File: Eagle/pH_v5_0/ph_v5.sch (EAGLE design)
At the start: 89 parts, among them CON1 JACK_DC_BARREL, IC1 MCP1703DB, J1 RJ12RIGHTANGLE-I2C, J2 RJ12RIGHTANGLE-I2C, Q5 BSP75, Q6 BSP75, U1 HX711, X2 16MHz, X3 FH12-08S-1SH, X4 MINI-USB

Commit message: new v4.3, removed bistable control of the stepper, now on pins A0/A1/D8/D9, control sequence must be adapted in the arduino code. Started to work on the ph_V5.0 board, need to add two steppers and the analog backend circuit
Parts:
- removed 5V1: (no value), Headerlibrary:PINHD-1X1
- removed C16, C17: 100nF, rcl:C-EUC1206
- removed CU5, CU6: 10uF, rcl:C-EUC1206
- removed D3, D5: 1N581D1206, lpatiny:1N581D1206
- removed IN, OUT: (no value), jumper:JP1E
- removed LDIN, LDOUT, LDPW5: RED, adafruit:LEDCHIP-LED0805
- removed Q5, Q6: BSP75, infineon:BSP613P
- removed R13: 1k, resistor:R-EU_R0805
- removed R5, R6, R8: 1K, rcl:R-EU_R0805
- removed U$2: NCP1117LPST50T3G, lpatiny:NCP1117LPST50T3G
- removed U$6: TXB0104, lpatiny:TXB0104
- added 100K: 100k, rcl:R-EU_R0805
- added AN_OUT, LORA_RST: (no value), Headerlibrary:PINHD-1X1
- added C3, C4: 100nF, rcl:C-EUC1206
- added JP2: M02PTH, SparkFun-Connectors:M02PTH
- added LDM1, LDM2, LDM3, LDM4, RXLD, TXLD: RED, adafruit:LEDCHIP-LED0805
- added Q1, Q2, Q3, Q4: BSP75, infineon:BSP613P
- added R10: 1K, rcl:R-EU_R0805
- added RK10, RK11, RK14, RK17, RK8, RK9: 10K, rcl:R-EU_R0805
- added RK15, RK16: 10k, rcl:R-EU_R0805
- added RT2: 4.7k, resistor:R-EU_R1206
- added SJ4, SJ5, SJ6: JUMPER-PAD-2-NC_BY_TRACE, SparkFun-Passives:JUMPER-PAD-2-NC_BY_TRACE
- added STEPPER: (no value), con-lsta:FE06-1
- added U$4: DS18B20, lpatiny:DS18B20
- added U100: RN2483, Octanis1:RN2483
- RK12, RK13: value 10k -> 10K
- X2: value 16MHz -> 8MHz
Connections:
- removed net +5V: CU5.1, D3.A, U$2.OUT, U$2.TAB_OUT
- removed net +5V/1: 32U4.AVCC, 32U4.AVCC1, 32U4.UVCC, 32U4.VCC, 32U4.VCC1, 5V1.1, BJ1.E, C1.1, C12.2, C17.2, C2.1, C6.1, CU1.1, CU3.1, CU4.1, CU7.1, D2.C, D3.C, D4.C, IC1.VI, J1.5, J2.5, R13.1, R8.2, RK1.1, RK18.1, RK19.1, RK2.1, RK5.2, RK6.2, U$6.VCCB, U1.DVDD, U1.VSUP, X3-1.1, X3-2.1
- removed net FMOSI: D5.A, RK4.1, U$1.MOSI
- removed net MISO3: U$1.MISO, U$6.A3
- removed net MOSI3: D5.C, U$6.A2
- removed net N$11: Q5.G, R6.2, RK13.2
- removed net N$12: LDPW5.A, R13.2
- removed net N$13: OUT.2, Q5.D@1
- removed net N$17: IN.2, Q6.D@1
- removed net N$27: LDIN.A, RK12.1
- removed net N$28: LDOUT.A, RK13.1
- removed net N$4: R8.1, U$6.OE
- removed net N$8: Q6.G, R5.2, RK12.2
- removed net SCK3: RK3.1, U$6.A4
- removed net SC_MEM: R3.2, U$6.NC
- new net ANGND: C3.2, C4.2, SJ4.2, SJ5.2, SJ6.2, U100.P$1, U100.P$11, U100.P$20, U100.P$21, U100.P$22, U100.P$24, U100.P$26, U100.P$27, U100.P$28, U100.P$33, U100.P$41, U100.P$47, U100.P$8
- new net ANT868: AN_OUT.1, U100.P$23
- new net B+: JP2.1, U1.INB+
- new net B-: JP2.2, U1.INB-
- new net N$14: Q4.D@1, RK8.1, STEPPER.1
- new net N$15: Q2.D@1, RK9.1, STEPPER.3
- new net N$16: Q3.D@1, RK10.1, STEPPER.4
- new net N$18: RK15.2, TXLD.A
- new net N$19: Q1.D@1, RK11.1, STEPPER.6
- new net N$24: RK16.2, RXLD.A
- new net N$31: LDM4.C, RK8.2
- new net N$32: LDM3.C, RK9.2
- new net N$33: LDM2.C, RK10.2
- new net N$37: LDM1.C, RK11.2
- new net N$9: R10.2, RT2.2, U$4.DQ
- net +12V: now also C1.1, C2.1, CU3.1, CU4.1, CU7.1, D2.C, D4.C, IC1.VI, LDM1.A, LDM2.A, LDM3.A, LDM4.A, STEPPER.2, STEPPER.5, X3-1.1, X3-2.1; no longer CU6.1, IN.1, OUT.1, U$2.IN
- net 3.3V: now also 100K.1, 32U4.AVCC, 32U4.AVCC1, 32U4.UVCC, 32U4.VCC, 32U4.VCC1, BJ1.E, C12.2, C3.1, C4.1, C6.1, CU1.1, RK1.1, RK15.1, RK16.1, RK18.1, RK19.1, RK2.1, RK5.2, RK6.2, RT2.1, U$4.VDD, U1.DVDD, U1.VSUP, U100.P$12, U100.P$34; no longer C16.2, U$6.VCCA
- net A0: now also Q2.G, RK13.2
- net A1: now also Q4.G, RK17.2
- net A2: now also Q3.G, RK14.2; no longer R5.1
- net A3: now also Q1.G, RK12.2; no longer R6.1
- net D10*: now also R3.2; no longer U$6.NC2
- net D5*: now also 100K.2, LORA_RST.1, U100.P$32
- net D6*: now also R10.1
- net GND: now also Q1.S, Q2.S, Q3.S, Q4.S, RK12.1, RK13.1, RK14.1, RK17.1, SJ4.1, SJ5.1, SJ6.1, U$4.GND; no longer C16.1, C17.1, CU5.2, CU6.2, LDIN.C, LDOUT.C, LDPW5.C, Q5.S, Q6.S, U$2.ADJ, U$6.GND
- net MISO: now also U$1.MISO; no longer U$6.B3
- net MOSI: now also RK4.1, U$1.MOSI; no longer U$6.B2
- net RX: now also U100.P$6
- net RXLED: now also RXLD.C
- net SCK: now also RK3.1; no longer U$6.B4
- net TX: now also U100.P$7
- net TXLED: now also TXLD.C
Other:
- note added: "LoRa RN2483"
- note added: "One wire"
- note added: "STEPPER"
- note removed: "5V LDO"
- note removed: "FOOD"
- note removed: "LEVEL_Converters"
- note removed: "PID"
- moved on the sheet: CU9, RK12, RK13, RUSB1, RUSB2, X4G$1

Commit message: started design of the phv5.0 board, conductommetry is still missing, stepper to be rerouted to use one single port would be better !
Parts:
- removed C9: 100nF, rcl:C-EUC1206
- removed JP2: M02PTH, SparkFun-Connectors:M02PTH
- removed R10: 1K, rcl:R-EU_R0805
- removed RL1, RL2: 100, resistor:R-EU_M0805
- removed RT2: 4.7k, resistor:R-EU_R1206
- removed U$4: DS18B20, lpatiny:DS18B20
- removed WGT: (no value), SparkFun-Connectors:M05PTH
- added C14, C15: 100n, rcl:C-EUC1206
- added C16: 22uF, rcl:C-EUC1206
- added IC2: TL084D, linear:TL084D
- added LDM5, LDM6, LDM7, LDM8: RED, adafruit:LEDCHIP-LED0805
- added Q5, Q6, Q7, Q8: BSP75, infineon:BSP613P
- added R4, R5, R9: 2.2k, resistor:R-EU_R0805
- added R6, R8: 100k, resistor:R-EU_R0805
- added STEPPER1: (no value), con-lsta:FE06-1
- added U$2: BNC-VERTICAL, phMeter:BNC-VERTICAL
- added U$3: VERTICAL-JACK, phMeter:VERTICAL-JACK
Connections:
- removed net N$20: C9.2, RL1.1, U1.INA-
- removed net N$43: C9.1, RL2.1, U1.INA+
- new net N$11: LDM6.C, RK13.2
- new net N$12: LDM7.C, RK14.2
- new net N$13: LDM8.C, RK17.2
- new net N$17: R4.2, R5.2, R9.1
- new net N$2: Q5.D@1, RK12.1, STEPPER1.1
- new net N$21: IC2B.+IN, U$2.OUT
- new net N$27: C15.2, IC2A.-IN, R6.1, R8.2
- new net N$28: IC2B.-IN, IC2B.OUT, R4.1
- new net N$4: Q7.D@1, RK13.1, STEPPER1.3
- new net N$6: Q6.D@1, RK14.1, STEPPER1.4
- new net N$8: Q8.D@1, RK17.1, STEPPER1.6
- net +12V: now also LDM5.A, LDM6.A, LDM7.A, LDM8.A, STEPPER1.2, STEPPER1.5
- net 3.3V: now also C14.1, IC2P.V+, R6.2; no longer RT2.1, U$4.VDD
- net A+: now also U1.INA+; no longer RL2.2, WGT.2
- net A-: now also U1.INA-; no longer RL1.2, WGT.3
- net A0: now also Q6.G; no longer Q2.G, RK13.2
- net A1: now also Q7.G; no longer Q4.G, RK17.2
- net A2: now also Q5.G; no longer Q3.G, RK14.2
- net A3: now also Q8.G; no longer Q1.G, RK12.2
- net A6: now also Q2.G
- net B+: now also C16.2, R9.2; no longer JP2.1
- net B-: now also IC2A.+IN, IC2A.OUT, U$2.GND; no longer JP2.2
- net D12*: now also Q3.G
- net D6*: now also Q1.G; no longer R10.1
- net D8*: now also Q4.G
- net GND: now also C14.2, C15.1, C16.1, IC2P.V-, Q5.S, Q6.S, Q7.S, Q8.S, R5.1, R8.1; no longer RK12.1, RK13.1, RK14.1, RK17.1, U$4.GND, WGT.1, WGT.4
- net N$5: no longer WGT.5
- net N$9: now also LDM5.C, RK12.2; no longer R10.2, RT2.2, U$4.DQ
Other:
- note removed: "One wire"
- moved on the sheet: 12V, 3V3, C10, GND, RK12, RK13, RK14, RK17

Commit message: ph board v5, need to be checked, to provide pin mapping and gerbers
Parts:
- removed RK15: 10k, rcl:R-EU_R0805
- removed SJ5: JUMPER-PAD-2-NC_BY_TRACE, SparkFun-Passives:JUMPER-PAD-2-NC_BY_TRACE
- removed TXLD: RED, adafruit:LEDCHIP-LED0805
- added B1: MB1S, rectifier:MB1S
- added C17, C18, C19, C20, C24, C9: 100nF, SparkysWidgets:CAP1206
- added C21, C22, C23: 1uF, SparkysWidgets:CAP1206
- added D3, D5: 4148, SparkysWidgets:MBR0520LT
- added IC3: TL084D, linear:TL084D
- added IC5: TPS60400DBV, SparkysWidgets:TPS60400DBV
- added R10: 22K, SparkysWidgets:RESISTOR0805-RES
- added R11, R13, R15, R16, R17, R18, R20, R21, R22, R23, R24: 1K, SparkysWidgets:RESISTOR0805-RES
- added R19: 1k, resistor:R-EU_R0805
- added R7: 10K, SparkysWidgets:RESISTOR0805-RES
- added TP5: OSCVout, SW_Passives:TEST-POINT3
- added U$5: BNC-VERTICAL, phMeter:BNC-VERTICAL
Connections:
- removed net A-: U1.INA-
- new net -3V3: C22.2, IC3P.V-, IC5.OUT
- new net N$20: C9.1, R13.1
- new net N$26: C19.1, IC3A.OUT, R10.2, R13.2, R15.1
- new net N$29: IC3B.+IN, R15.2, R16.1, TP5.1
- new net N$30: C17.2, C9.2, IC3A.+IN, R11.2
- new net N$35: IC3B.-IN, R18.1, U$5.OUT
- new net N$36: C24.1, IC3B.OUT, R18.2
- new net N$40: C24.2, IC3C.+IN, R20.2
- new net N$43: B1.AC2, IC3C.OUT
- new net N$44: C19.2, D3.C, D5.A
- new net N$45: C21.1, IC5.CFLY-
- new net N$46: C21.2, IC5.CFLY+
- new net N$47: B1.-, C18.1, R17.1, R23.1
- new net N$48: B1.AC1, IC3C.-IN, R21.1
- new net N$49: B1.+, C18.2, R17.2, R22.1
- new net N$50: IC3D.+IN, R22.2
- new net N$51: IC3D.-IN, R23.2, R24.2
- net 3.3V: now also C20.1, C23.1, IC3P.V+, IC5.IN, U$3.1; no longer RK15.1
- net A+: now also IC3D.OUT, R24.1
- net A4: now also R19.1, U$3.2; no longer U1.DOUT
- net ANGND: no longer SJ5.2
- net D7*: now also U1.DOUT
- net D8*: no longer Q4.G
- net GND: now also C17.1, C20.2, C22.1, C23.2, IC5.GND, R11.1, R16.2, R19.2, R20.1, R21.2, R7.1, U$5.GND; no longer SJ5.1
- net LGND: now also U1.INA-
- net N$18: now also D3.A, D5.C, IC3A.-IN, R10.1, R7.2; no longer RK15.2, TXLD.A
- net TXLED: now also Q4.G; no longer TXLD.C
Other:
- note added: "24bits ADC HX711"
- note added: "Basic AGC with 2 diodes and a cap"
- note added: "Basic Wein Bridge Oscillator"
- note added: "Charge pump, negative voltage gen"
- note added: "Gain ~= 3, R4/R3 ~=2"
- note added: "OSCVout should be ~120mV Lower = better more gain room, but enough to drive probe"
- note added: "OSCfq=1/(2piR16C4)"
- note added: "R15= R16 and C4= C5 (forms bandpass) Positive feedback at bandpass (osc) Fq"
- note added: "conductometer"
- note added: "pH"
- note removed: "A+"
- note removed: "A-"
- note removed: "Black"
- note removed: "E+"
- note removed: "E-"
- note removed: "Load cell 24bits ADC"
- note removed: "Red"
- note removed: "Shield"
- note removed: "White"
- note removed: "Yellow"
- moved on the sheet: 20K, 8.2K, BJ1, C14, C15, C16, C6, C7, C8, CU1, CU2, IC2A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

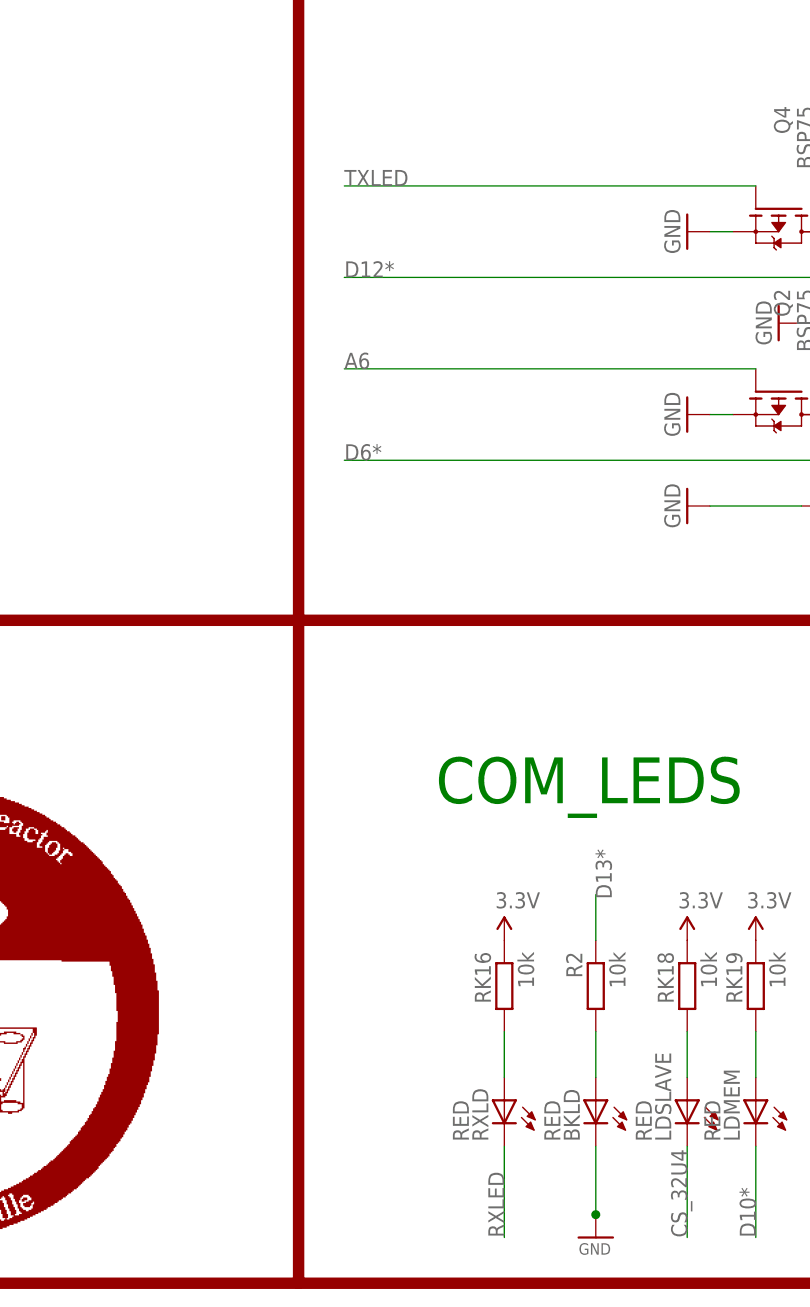
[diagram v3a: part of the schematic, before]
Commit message: finished phv5.0 board, need to dimension correctly the pH resistors and conductometry resistors and capa (not dimensionned yet !! careful not to solder anything)
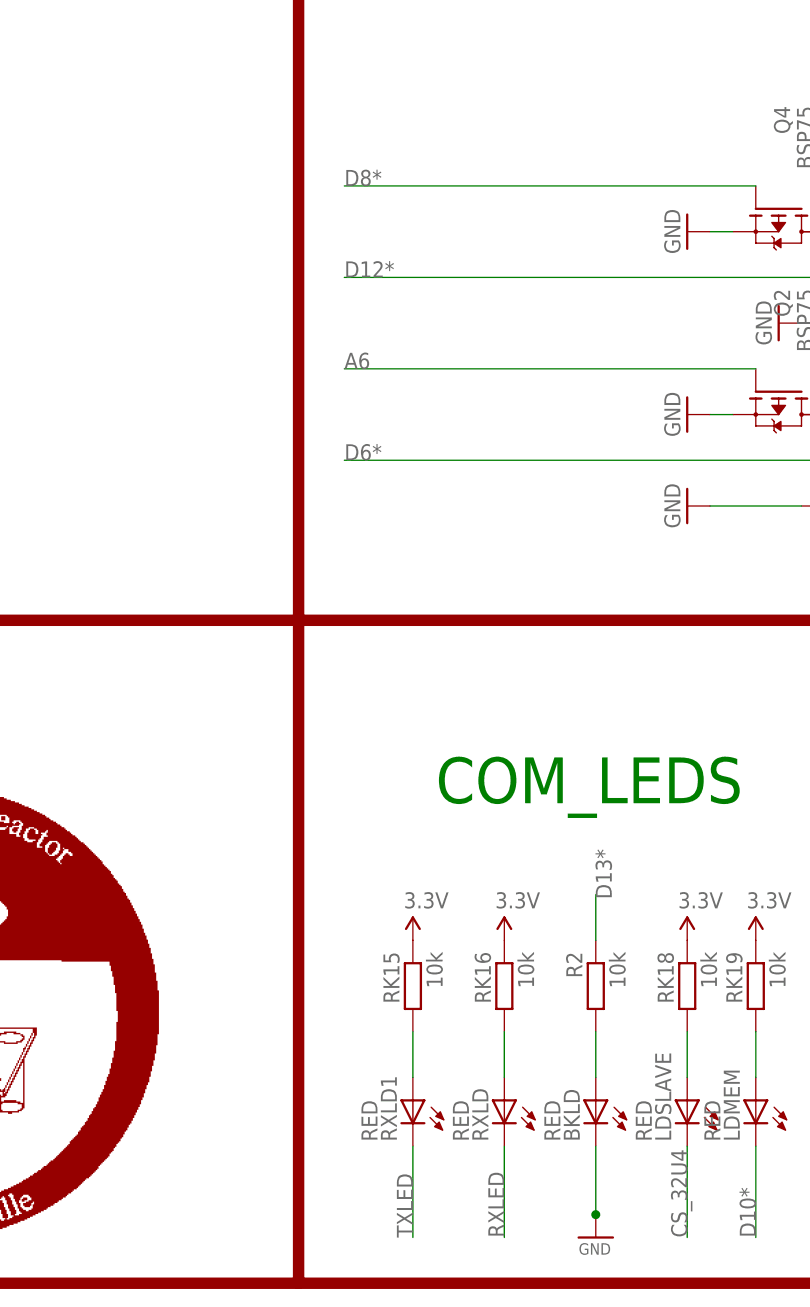
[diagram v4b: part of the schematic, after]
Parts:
- added RK15: 10k, rcl:R-EU_R0805
- added RXLD1: RED, adafruit:LEDCHIP-LED0805
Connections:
- new net N$52: RK15.2, RXLD1.A
- net 3.3V: now also RK15.1
- net D8*: now also Q4.G
- net TXLED: now also RXLD1.C; no longer Q4.G
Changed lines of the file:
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@@
 <grid distance="0.1" unitdist="inch" unit="inch" style="lines" multiple="1" display="no" altdistance="0.01" altunitdist="inch" altunit="inch"/>
 <layers>
-<layer number="1" name="Top" color="4" fill="1" visible="yes" active="no"/>
-<layer number="16" name="Bottom" color="1" fill="1" visible="yes" active="no"/>
-<layer number="17" name="Pads" color="2" fill="1" visible="yes" active="no"/>
-<layer number="18" name="Vias" color="2" fill="1" visible="yes" active="no"/>
-<layer number="19" name="Unrouted" color="6" fill="1" visible="yes" active="no"/>
-<layer number="20" name="Dimension" color="15" fill="1" visible="yes" active="no"/>
-<layer number="21" name="tPlace" color="7" fill="1" visible="yes" active="no"/>
-<layer number="22" name="bPlace" color="7" fill="1" visible="yes" active="no"/>
-<layer number="23" name="tOrigins" color="15" fill="1" visible="yes" active="no"/>
-<layer number="24" name="bOrigins" color="15" fill="1" visible="yes" active="no"/>
-<layer number="25" name="tNames" color="7" fill="1" visible="yes" active="no"/>
-<layer number="26" name="bNames" color="7" fill="1" visible="yes" active="no"/>
-<layer number="27" name="tValues" color="7" fill="1" visible="yes" active="no"/>
-<layer number="28" name="bValues" color="7" fill="1" visible="yes" active="no"/>
+<layer number="1" name="Top" color="4" fill="1" visible="no" active="no"/>
+<layer number="16" name="Bottom" color="1" fill="1" visible="no" active="no"/>
+<layer number="17" name="Pads" color="2" fill="1" visible="no" active="no"/>
+<layer number="18" name="Vias" color="2" fill="1" visible="no" active="no"/>
+<layer number="19" name="Unrouted" color="6" fill="1" visible="no" active="no"/>
+<layer number="20" name="Dimension" color="15" fill="1" visible="no" active="no"/>
+<layer number="21" name="tPlace" color="7" fill="1" visible="no" active="no"/>
+<layer number="22" name="bPlace" color="7" fill="1" visible="no" active="no"/>
+<layer number="23" name="tOrigins" color="15" fill="1" visible="no" active="no"/>
+<layer number="24" name="bOrigins" color="15" fill="1" visible="no" active="no"/>
+<layer number="25" name="tNames" color="7" fill="1" visible="no" active="no"/>
+<layer number="26" name="bNames" color="7" fill="1" visible="no" active="no"/>
+<layer number="27" name="tValues" color="7" fill="1" visible="no" active="no"/>
+<layer number="28" name="bValues" color="7" fill="1" visible="no" active="no"/>
 <layer number="29" name="tStop" color="7" fill="3" visible="no" active="no"/>
 <layer number="30" name="bStop" color="7" fill="6" visible="no" active="no"/>
@@
 <layer number="35" name="tGlue" color="7" fill="4" visible="no" active="no"/>
 <layer number="36" name="bGlue" color="7" fill="5" visible="no" active="no"/>
-<layer number="37" name="tTest" color="7" fill="1" visible="yes" active="no"/>
-<layer number="38" name="bTest" color="7" fill="1" visible="yes" active="no"/>
+<layer number="37" name="tTest" color="7" fill="1" visible="no" active="no"/>
+<layer number="38" name="bTest" color="7" fill="1" visible="no" active="no"/>
 <layer number="39" name="tKeepout" color="4" fill="11" visible="no" active="no"/>
 <layer number="40" name="bKeepout" color="1" fill="11" visible="no" active="no"/>
@@
 <layer number="44" name="Drills" color="7" fill="1" visible="no" active="no"/>
 <layer number="45" name="Holes" color="7" fill="1" visible="no" active="no"/>
-<layer number="46" name="Milling" color="3" fill="1" visible="yes" active="no"/>
-<layer number="47" name="Measures" color="7" fill="1" visible="yes" active="no"/>
-<layer number="48" name="Document" color="7" fill="1" visible="yes" active="no"/>
-<layer number="49" name="Reference" color="7" fill="1" visible="yes" active="no"/>
-<layer number="50" name="dxf" color="12" fill="1" visible="yes" active="no"/>
-<layer number="51" name="tDocu" color="7" fill="1" visible="yes" active="no"/>
-<layer number="52" name="bDocu" color="7" fill="1" visible="yes" active="no"/>
-<layer number="53" name="tGND_GNDA" color="7" fill="1" visible="yes" active="no"/>
-<layer number="54" name="bGND_GNDA" color="7" fill="1" visible="yes" active="no"/>
-<layer number="56" name="wert" color="7" fill="1" visible="yes" active="no"/>
-<layer number="57" name="tCAD" color="7" fill="1" visible="yes" active="no"/>
-<layer number="59" name="tCarbon" color="7" fill="1" visible="yes" active="no"/>
-<layer number="60" name="bCarbon" color="7" fill="1" visible="yes" active="no"/>
+<layer number="46" name="Milling" color="3" fill="1" visible="no" active="no"/>
+<layer number="47" name="Measures" color="7" fill="1" visible="no" active="no"/>
+<layer number="48" name="Document" color="7" fill="1" visible="no" active="no"/>
+<layer number="49" name="Reference" color="7" fill="1" visible="no" active="no"/>
+<layer number="50" name="dxf" color="12" fill="1" visible="no" active="no"/>
+<layer number="51" name="tDocu" color="7" fill="1" visible="no" active="no"/>
+<layer number="52" name="bDocu" color="7" fill="1" visible="no" active="no"/>
+<layer number="53" name="tGND_GNDA" color="7" fill="1" visible="no" active="no"/>
+<layer number="54" name="bGND_GNDA" color="7" fill="1" visible="no" active="no"/>
+<layer number="56" name="wert" color="7" fill="1" visible="no" active="no"/>
+<layer number="57" name="tCAD" color="7" fill="1" visible="no" active="no"/>
+<layer number="59" name="tCarbon" color="7" fill="1" visible="no" active="no"/>
+<layer number="60" name="bCarbon" color="7" fill="1" visible="no" active="no"/>
 <layer number="90" name="Modules" color="5" fill="1" visible="no" active="no"/>
 <layer number="91" name="Nets" color="2" fill="1" visible="yes" active="yes"/>
@@
 <part name="R23" library="SparkysWidgets" deviceset="RESISTOR" device="0805-RES" value="1K"/>
 <part name="R24" library="SparkysWidgets" deviceset="RESISTOR" device="0805-RES" value="1K"/>
+<part name="RXLD1" library="adafruit" deviceset="LED" device="CHIP-LED0805" value="RED"/>
+<part name="RK15" library="rcl" deviceset="R-EU_" device="R0805" value="10k"/>
+<part name="P+46" library="SparkFun" deviceset="3.3V" device=""/>
 </parts>
 <sheets>
@@
 <attribute name="VALUE" x="151.13" y="117.602" size="1.778" layer="96" rot="R180"/>
 </instance>
+<instance part="RXLD1" gate="G$1" x="398.78" y="27.94" rot="MR0"/>
+<instance part="RK15" gate="G$1" x="398.78" y="40.64" rot="MR270"/>
+<instance part="P+46" gate="G$1" x="398.78" y="45.72"/>
 </instances>
 <busses>
@@
 </segment>
 <segment>
-<pinref part="Q4" gate="G$1" pin="G"/>
-<wire x1="436.88" y1="129.54" x2="391.16" y2="129.54" width="0.1524" layer="91"/>
-<label x="391.16" y="129.54" size="1.778" layer="95"/>
+<pinref part="RXLD1" gate="G$1" pin="C"/>
+<wire x1="398.78" y1="22.86" x2="398.78" y2="12.7" width="0.1524" layer="91"/>
+<label x="398.78" y="12.7" size="1.778" layer="95" rot="R90"/>
 </segment>
 </net>
@@
 <pinref part="P+45" gate="G$1" pin="3.3V"/>
 </segment>
+<segment>
+<pinref part="RK15" gate="G$1" pin="1"/>
+<pinref part="P+46" gate="G$1" pin="3.3V"/>
+</segment>
 </net>
 <net name="N$10" class="0">
@@
 <label x="345.44" y="142.24" size="1.778" layer="95"/>
 </segment>
+<segment>
+<pinref part="Q4" gate="G$1" pin="G"/>
+<wire x1="436.88" y1="129.54" x2="391.16" y2="129.54" width="0.1524" layer="91"/>
+<label x="391.16" y="129.54" size="1.778" layer="95"/>
+</segment>
 </net>
 <net name="RESET" class="0">
@@
 </segment>
 </net>
+<net name="N$52" class="0">
+<segment>
+<pinref part="RK15" gate="G$1" pin="2"/>
+<pinref part="RXLD1" gate="G$1" pin="A"/>
+<wire x1="398.78" y1="30.48" x2="398.78" y2="35.56" width="0.1524" layer="91"/>
+</segment>
+</net>
